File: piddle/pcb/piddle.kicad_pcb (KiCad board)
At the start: 2 copper layers, 118 x 104.8 mm, 42 parts, among them J1 Conn_01x03_Socket, J10 Conn_01x03_Socket, J2 Conn_01x03_Socket, J3 Conn_01x03_Socket, J4 Conn_01x03_Socket, J5 Conn_01x03_Socket, J6 Conn_01x03_Socket, J7 Conn_01x03_Socket, J8 Conn_01x03_Socket, J9 Conn_01x03_Socket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

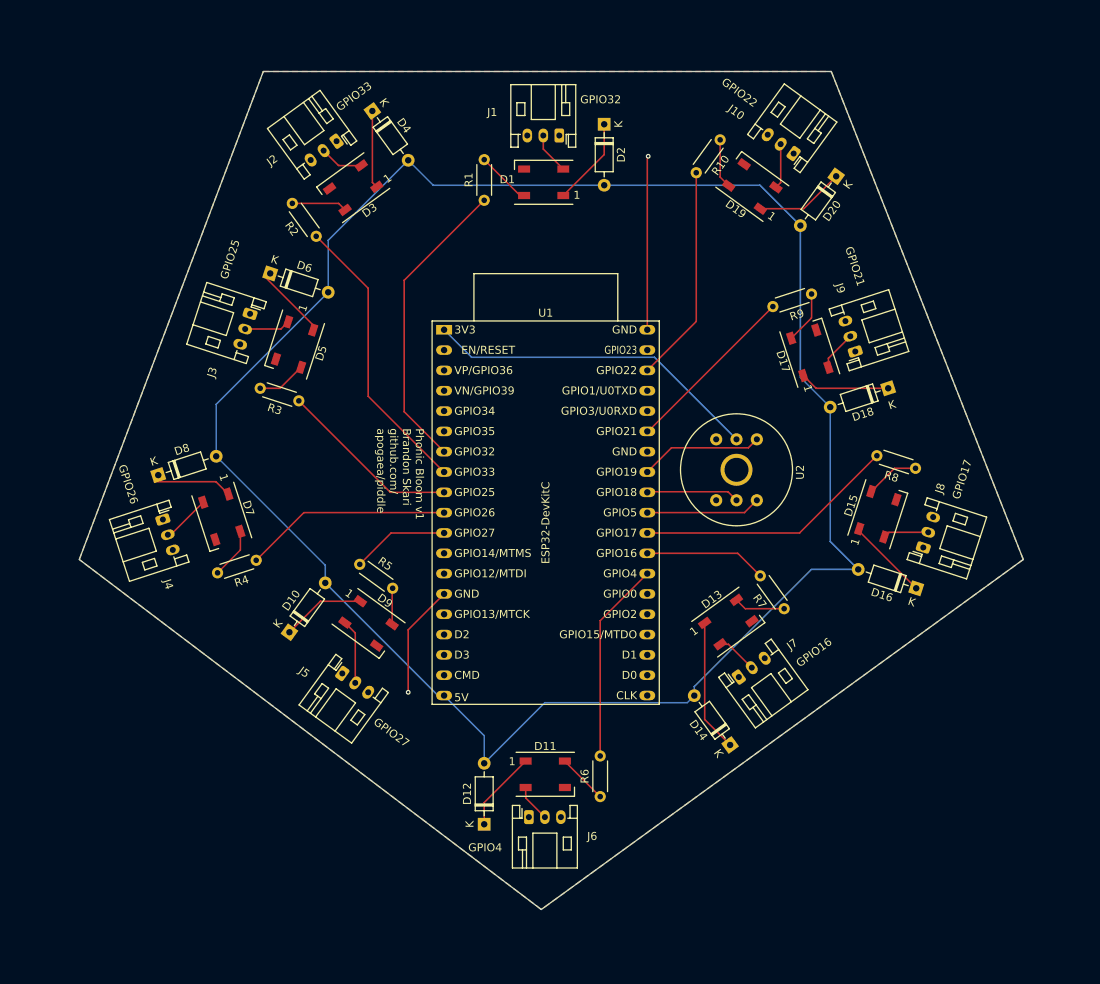
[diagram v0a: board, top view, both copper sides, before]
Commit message: Pigtail strain relief mounting holes
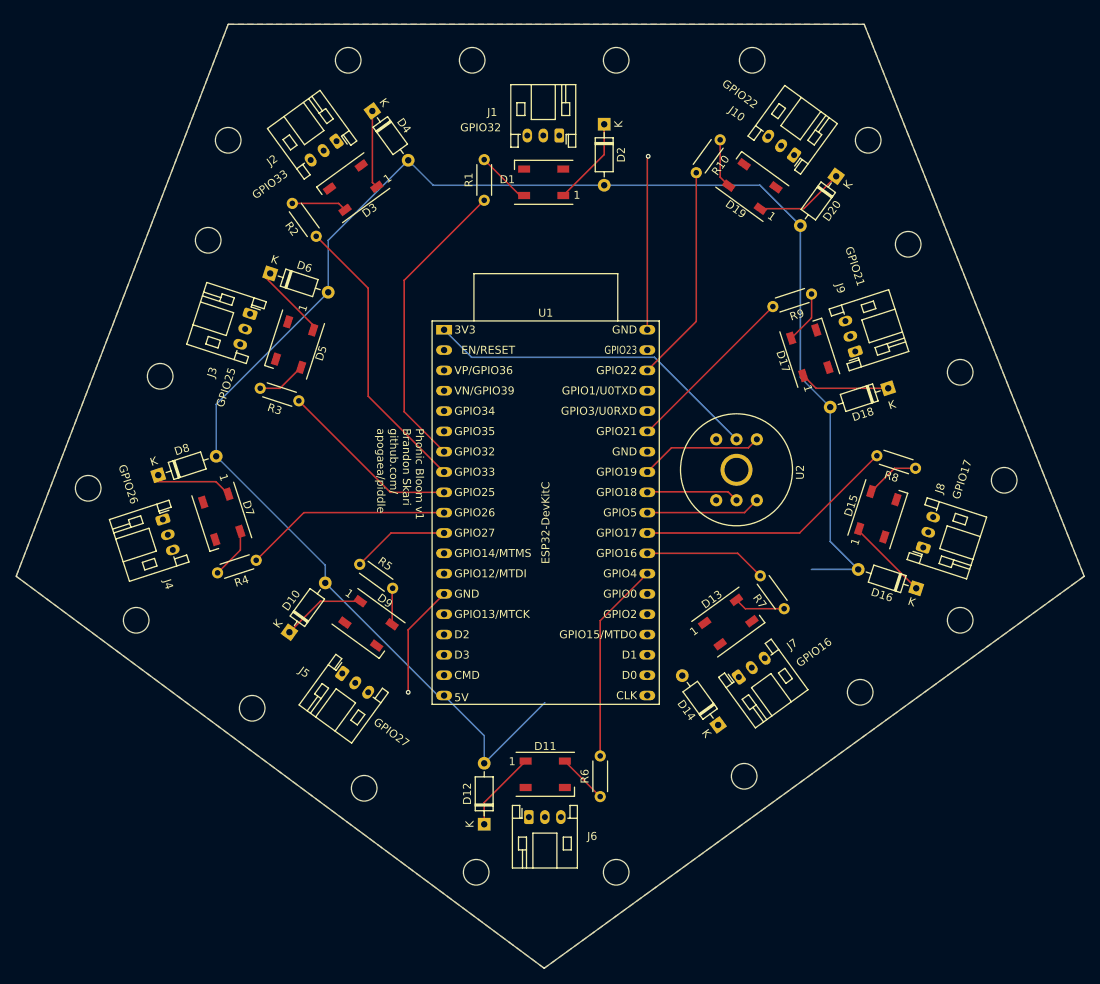
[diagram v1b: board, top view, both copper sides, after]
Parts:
- added REF**: MountingHole_3.2mm_M3, MountingHole:MountingHole_3.2mm_M3, F.Cu at (157.1, 97.6)
- added REF**: MountingHole_3.2mm_M3, MountingHole:MountingHole_3.2mm_M3, F.Cu at (80.6, 58.6)
- added REF**: MountingHole_3.2mm_M3, MountingHole:MountingHole_3.2mm_M3, F.Cu at (114.1, 58.6)
- added REF**: MountingHole_3.2mm_M3, MountingHole:MountingHole_3.2mm_M3, F.Cu at (96.1, 58.6)
- added REF**: MountingHole_3.2mm_M3, MountingHole:MountingHole_3.2mm_M3, F.Cu at (114.1, 160.1)
- added REF**: MountingHole_3.2mm_M3, MountingHole:MountingHole_3.2mm_M3, F.Cu at (144.6, 137.6)
- added REF**: MountingHole_3.2mm_M3, MountingHole:MountingHole_3.2mm_M3, F.Cu at (54.1, 128.6)
- added REF**: MountingHole_3.2mm_M3, MountingHole:MountingHole_3.2mm_M3, F.Cu at (162.6, 111.1)
- added REF**: MountingHole_3.2mm_M3, MountingHole:MountingHole_3.2mm_M3, F.Cu at (131.1, 58.6)
- added REF**: MountingHole_3.2mm_M3, MountingHole:MountingHole_3.2mm_M3, F.Cu at (63.1, 81.1)
- added REF**: MountingHole_3.2mm_M3, MountingHole:MountingHole_3.2mm_M3, F.Cu at (82.6, 149.6)
- added REF**: MountingHole_3.2mm_M3, MountingHole:MountingHole_3.2mm_M3, F.Cu at (157.1, 128.6)
- added REF**: MountingHole_3.2mm_M3, MountingHole:MountingHole_3.2mm_M3, F.Cu at (150.6, 81.6)
- added REF**: MountingHole_3.2mm_M3, MountingHole:MountingHole_3.2mm_M3, F.Cu at (145.6, 68.6)
- added REF**: MountingHole_3.2mm_M3, MountingHole:MountingHole_3.2mm_M3, F.Cu at (96.6, 160.1)
- added REF**: MountingHole_3.2mm_M3, MountingHole:MountingHole_3.2mm_M3, F.Cu at (130.1, 148.1)
- added REF**: MountingHole_3.2mm_M3, MountingHole:MountingHole_3.2mm_M3, F.Cu at (68.6, 139.6)
- added REF**: MountingHole_3.2mm_M3, MountingHole:MountingHole_3.2mm_M3, F.Cu at (48.1, 112.1)
- added REF**: MountingHole_3.2mm_M3, MountingHole:MountingHole_3.2mm_M3, F.Cu at (65.6, 68.6)
- added REF**: MountingHole_3.2mm_M3, MountingHole:MountingHole_3.2mm_M3, F.Cu at (57.1, 98.1)
- moved D14 2.92 mm to (126.9, 141.7)
- moved J10 0.20 mm to (136.3, 70.4)
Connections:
- net /3V3 renamed +3.3V
- net /5V renamed +5V
- net /GND renamed GND
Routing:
- net +5V: track 255.5 -> 214.6 mm
- net Net-(D13-VDD): track 16.6 -> 0.00 mm
- net Net-(D9-DOUT): track 8.07 -> 0.00 mm
- net Net-(D7-DOUT): track 6.10 -> 0.36 mm
- net Net-(D5-DOUT): track 5.74 -> 0.00 mm
- net Net-(D15-DOUT): track 5.73 -> 0.00 mm
- net Net-(D19-DOUT): track 5.64 -> 0.00 mm
- net Net-(D3-DOUT): track 5.48 -> 0.00 mm
- net Net-(D1-DOUT): track 5.24 -> 0.00 mm
- net Net-(D13-DOUT): track 5.16 -> 0.00 mm
- net Net-(D17-DOUT): track 5.02 -> 0.00 mm
- net Net-(D11-DOUT): track 4.69 -> 0.00 mm
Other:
- board size 118 x 104.8 mm -> 133.5 x 118 mm
- board text removed: "GPIO4"

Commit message: Grounds for LED strips
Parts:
- moved REF** 0.50 mm to (95.6, 58.6)
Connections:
- J1 pad 1: unconnected-(J1-Pin_1-Pad1) -> GND
- J10 pad 1: unconnected-(J10-Pin_1-Pad1) -> GND
- J2 pad 1: unconnected-(J2-Pin_1-Pad1) -> GND
- J3 pad 1: unconnected-(J3-Pin_1-Pad1) -> GND
- J4 pad 1: unconnected-(J4-Pin_1-Pad1) -> GND
- J5 pad 1: unconnected-(J5-Pin_1-Pad1) -> GND
- J6 pad 1: unconnected-(J6-Pin_1-Pad1) -> GND
- J7 pad 1: unconnected-(J7-Pin_1-Pad1) -> GND
- J8 pad 1: unconnected-(J8-Pin_1-Pad1) -> GND
- J9 pad 1: unconnected-(J9-Pin_1-Pad1) -> GND
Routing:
- net Net-(D9-DOUT): track 0.00 -> 8.07 mm
- net Net-(D7-DOUT): track 0.36 -> 6.10 mm
- net Net-(D5-DOUT): track 0.00 -> 5.74 mm
- net Net-(D15-DOUT): track 0.00 -> 5.73 mm
- net Net-(D3-DOUT): track 0.00 -> 5.48 mm
- net Net-(D19-DOUT): track 0.00 -> 5.48 mm
- net Net-(D1-DOUT): track 0.00 -> 5.24 mm
- net Net-(D13-DOUT): track 0.00 -> 5.16 mm
- net Net-(D17-DOUT): track 0.00 -> 5.02 mm
- net Net-(D11-DOUT): track 0.00 -> 4.69 mm

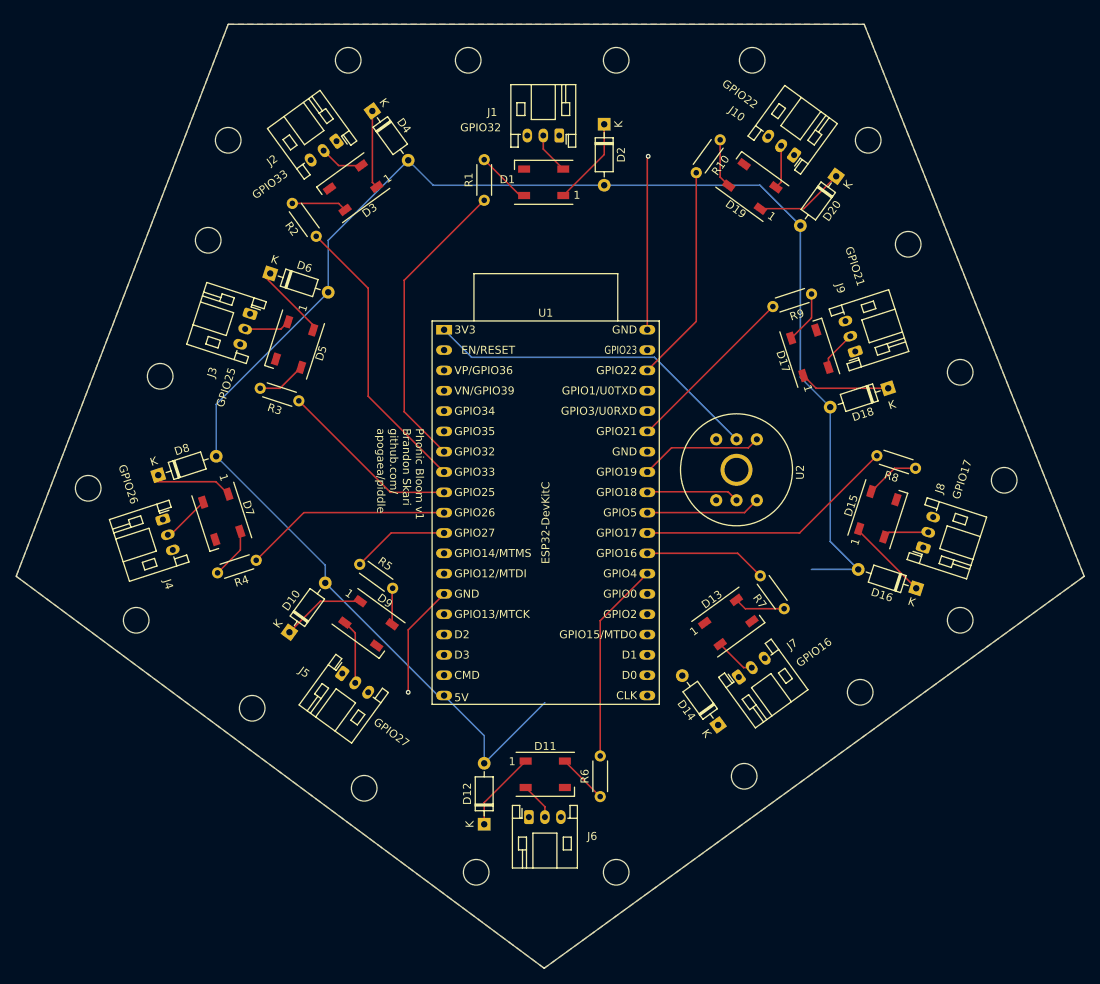
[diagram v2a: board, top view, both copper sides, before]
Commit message: Add power connectors
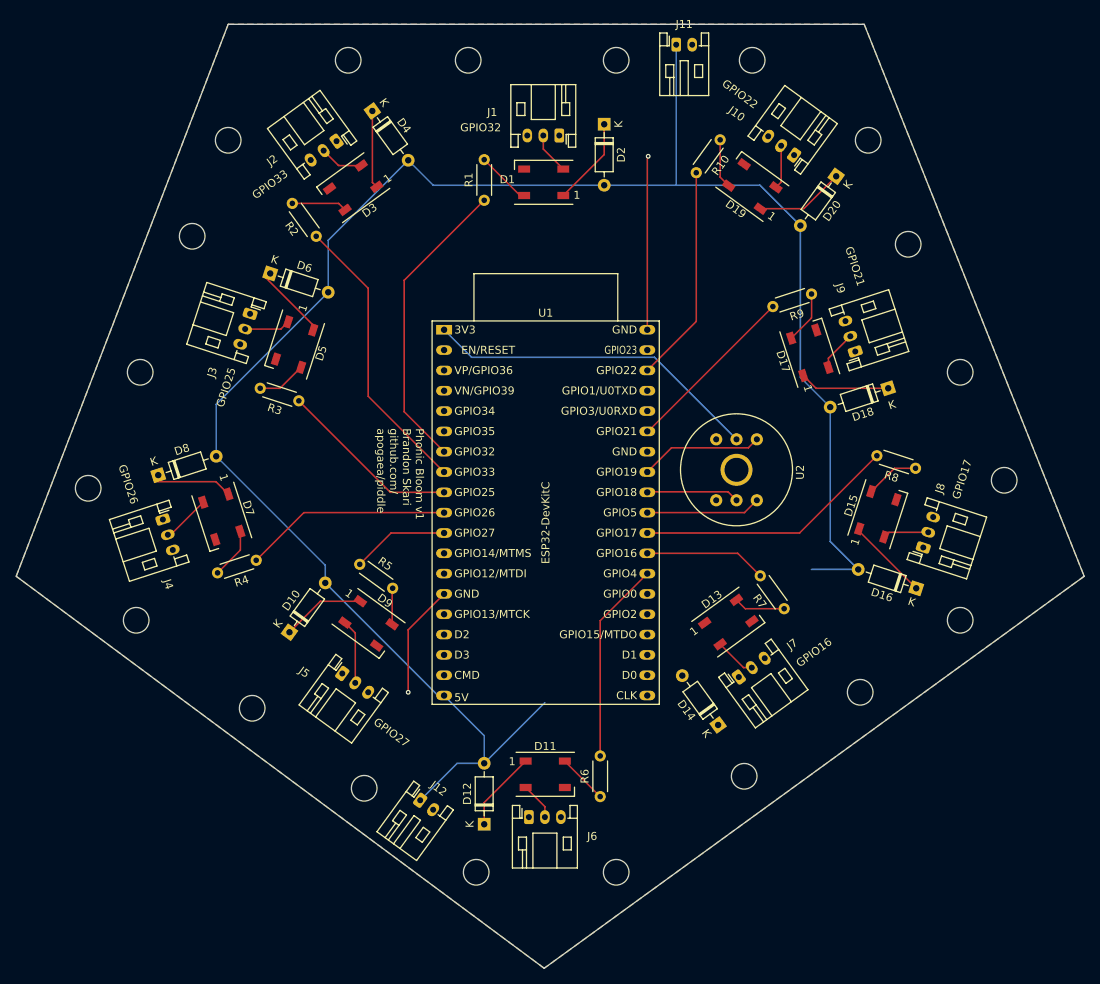
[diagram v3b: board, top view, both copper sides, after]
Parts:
- added J11: Conn_01x02_Socket, Connector_JST:JST_PH_S2B-PH-K_1x02_P2.00mm_Horizontal, F.Cu at (121.6, 56.6)
- added J12: Conn_01x02_Socket, Connector_JST:JST_PH_S2B-PH-K_1x02_P2.00mm_Horizontal, F.Cu at (89.6, 151.1)
- moved REF** 2.55 mm to (54.6, 97.6)
- moved REF** 2.06 mm to (61.1, 80.6)
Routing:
- net +5V: track 214.6 -> 242.1 mm
